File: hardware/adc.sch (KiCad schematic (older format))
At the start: 38 parts, among them U39 LP5907-3.0, U8 LTC2292

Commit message: Current working version.
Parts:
- removed C219, C30: 100n, fmcw3:C_0402b, symbol C
- C163, C164, C165, C166, C167, C168, C221, C223, C224, C225, C23, C24, C25, C27: footprint fmcw3:C_0402b -> Capacitor_SMD:C_0402_1005Metric; symbol C -> Device:C
- C19, C20, C216, C217, C218, C22, C220, C222, C249, C31: footprint fmcw3:C_0603b -> Capacitor_SMD:C_0603_1608Metric; symbol C -> Device:C
- C248: footprint fmcw3:C_0805b -> Capacitor_SMD:C_0805_2012Metric; symbol C -> Device:C
- R100, R20, R21, R91, R92, R93, R97, R98, R99: symbol R -> Device:R
- U39: symbol LP5907 -> fmcw3-rescue:LP5907
- U8: footprint Housings_DFN_QFN:QFN-64-1EP_9x9mm_Pitch0.5mm -> Package_DFN_QFN:QFN-64-1EP_9x9mm_P0.5mm_EP4.85x4.85mm; symbol LTC229X -> fmcw3-rescue:LTC229X
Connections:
- wire segments 120 -> 154

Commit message: Dropped the 3 from the end of the project name.
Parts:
- R100, R20, R21, R91, R92, R93, R97, R98, R99: footprint fmcw3:R_0402b -> fmcw:R_0402b
- U39: footprint fmcw3:SOT-23-5 -> fmcw:SOT-23-5; symbol fmcw3-rescue:LP5907 -> fmcw-rescue:LP5907-fmcw3-rescue
- U8: symbol fmcw3-rescue:LTC229X -> fmcw-rescue:LTC229X-fmcw3-rescue
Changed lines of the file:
@@
 EESchema Schematic File Version 4
-LIBS:fmcw3-cache
+LIBS:fmcw-cache
 EELAYER 26 0
 EELAYER END
@@
 F 0 "R93" V 4680 4950 50  0000 C CNN
 F 1 "0" V 4600 4950 50  0000 C CNN
-F 2 "fmcw3:R_0402b" V 4530 4950 30  0001 C CNN
+F 2 "fmcw:R_0402b" V 4530 4950 30  0001 C CNN
 F 3 "" H 4600 4950 30  0000 C CNN
 	1    4600 4950
@@
 F 0 "R91" V 2930 4700 50  0000 C CNN
 F 1 "0" V 2850 4700 50  0000 C CNN
-F 2 "fmcw3:R_0402b" V 2780 4700 30  0001 C CNN
+F 2 "fmcw:R_0402b" V 2780 4700 30  0001 C CNN
 F 3 "" H 2850 4700 30  0000 C CNN
 	1    2850 4700
@@
 F 0 "R92" V 2930 5100 50  0000 C CNN
 F 1 "DNP" V 2850 5100 50  0000 C CNN
-F 2 "fmcw3:R_0402b" V 2780 5100 30  0001 C CNN
+F 2 "fmcw:R_0402b" V 2780 5100 30  0001 C CNN
 F 3 "" H 2850 5100 30  0000 C CNN
 	1    2850 5100
@@
 OVDD
 $Comp
-L fmcw3-rescue:LP5907 U39
+L fmcw-rescue:LP5907-fmcw3-rescue U39
 U 1 1 58526584
 P 2800 1400
 F 0 "U39" H 3000 1200 60  0000 C CNN
 F 1 "LP5907-3.0" H 2900 1600 60  0000 C CNN
-F 2 "fmcw3:SOT-23-5" H 2800 1450 60  0001 C CNN
+F 2 "fmcw:SOT-23-5" H 2800 1450 60  0001 C CNN
 F 3 "" H 2800 1450 60  0000 C CNN
 	1    2800 1400
@@
 REFLA
 $Comp
-L fmcw3-rescue:LTC229X U8
+L fmcw-rescue:LTC229X-fmcw3-rescue U8
 U 1 1 59439276
 P 5950 4350
@@
 F 0 "R21" V 4680 3100 50  0000 C CNN
 F 1 "22" V 4600 3100 50  0000 C CNN
-F 2 "fmcw3:R_0402b" V 4530 3100 30  0001 C CNN
+F 2 "fmcw:R_0402b" V 4530 3100 30  0001 C CNN
 F 3 "" H 4600 3100 30  0000 C CNN
 	1    4600 3100
@@
 F 0 "R20" V 4430 5050 50  0000 C CNN
 F 1 "0" V 4350 5050 50  0000 C CNN
-F 2 "fmcw3:R_0402b" V 4280 5050 30  0001 C CNN
+F 2 "fmcw:R_0402b" V 4280 5050 30  0001 C CNN
 F 3 "" H 4350 5050 30  0000 C CNN
 	1    4350 5050
@@
 F 0 "R97" V 1430 2750 50  0000 C CNN
 F 1 "49.9" V 1350 2750 50  0000 C CNN
-F 2 "fmcw3:R_0402b" V 1280 2750 30  0001 C CNN
+F 2 "fmcw:R_0402b" V 1280 2750 30  0001 C CNN
 F 3 "" H 1350 2750 30  0000 C CNN
 	1    1350 2750
@@
 F 0 "R99" V 1730 2850 50  0000 C CNN
 F 1 "49.9" V 1650 2850 50  0000 C CNN
-F 2 "fmcw3:R_0402b" V 1580 2850 30  0001 C CNN
+F 2 "fmcw:R_0402b" V 1580 2850 30  0001 C CNN
 F 3 "" H 1650 2850 30  0000 C CNN
 	1    1650 2850
@@
 F 0 "R98" V 1430 4150 50  0000 C CNN
 F 1 "49.9" V 1350 4150 50  0000 C CNN
-F 2 "fmcw3:R_0402b" V 1280 4150 30  0001 C CNN
+F 2 "fmcw:R_0402b" V 1280 4150 30  0001 C CNN
 F 3 "" H 1350 4150 30  0000 C CNN
 	1    1350 4150
@@
 F 0 "R100" V 1730 4250 50  0000 C CNN
 F 1 "49.9" V 1650 4250 50  0000 C CNN
-F 2 "fmcw3:R_0402b" V 1580 4250 30  0001 C CNN
+F 2 "fmcw:R_0402b" V 1580 4250 30  0001 C CNN
 F 3 "" H 1650 4250 30  0000 C CNN
 	1    1650 4250

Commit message: Documentation for TPS5420D buck converter.
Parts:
- C248: MFN (none) -> 885012107014
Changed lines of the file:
@@
 F 2 "Capacitor_SMD:C_0805_2012Metric" H 1888 1400 30  0001 C CNN
 F 3 "" H 1850 1550 60  0000 C CNN
+F 4 "885012107014" H 0   0   50  0001 C CNN "MFN"
 	1    1850 1550
 	1    0    0    -1

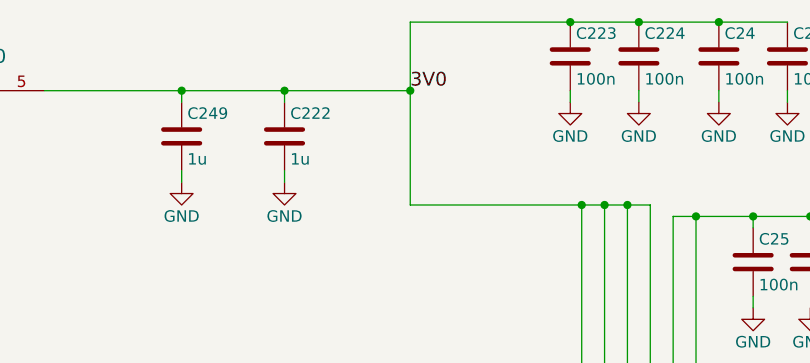
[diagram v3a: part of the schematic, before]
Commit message: Improved top level documentation.
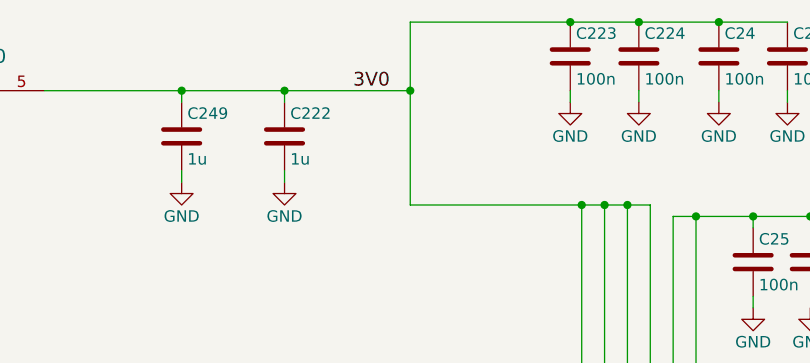
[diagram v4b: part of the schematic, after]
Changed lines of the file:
@@
 Text Label 2850 4450 0    60   ~ 0
 3V0
-Text Label 4900 1350 0    60   ~ 0
+Text Label 4650 1350 0    60   ~ 0
 3V0
 Text HLabel 7250 4100 2    60   Output ~ 0

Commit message: Added MFNs to components.
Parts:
- C163, C164, C165, C166, C167, C168: MFN (none) -> UMK105CG101JVHF
- C19, C20, C217, C218, C222, C249: MFN (none) -> CL10B105MO8NNWC
- C216, C22, C220, C31: MFN (none) -> CL10A225KO8NNNC
- C221, C223, C224, C225, C23, C24, C25, C27: MFN (none) -> CL05B104KO5NNNC
- C248: MFN 885012107014 -> CL21B106KQQNNNE
- R100, R97, R98, R99: footprint fmcw:R_0402b -> Resistor_SMD:R_0402_1005Metric; MFN (none) -> ERJ-2RKF49R9X
- R20, R91, R93: footprint fmcw:R_0402b -> Resistor_SMD:R_0402_1005Metric; MFN (none) -> ERJ-2GE0R00X
- R21: footprint fmcw:R_0402b -> Resistor_SMD:R_0402_1005Metric; MFN (none) -> ERJ-2RKF22R0X
- R92: footprint fmcw:R_0402b -> Resistor_SMD:R_0402_1005Metric
- U39: footprint fmcw:SOT-23-5 -> Package_TO_SOT_SMD:SOT-23-5; MFN (none) -> LP5907MFX-3.0/NOPB
- U8: MFN (none) -> LTC2292IUP#PBF
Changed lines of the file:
@@
 F 2 "Capacitor_SMD:C_0402_1005Metric" H 5638 1050 30  0001 C CNN
 F 3 "" H 5600 1200 60  0000 C CNN
+F 4 "CL05B104KO5NNNC" H 0   0   50  0001 C CNN "MFN"
 	1    5600 1200
 	1    0    0    -1
@@
 F 2 "Capacitor_SMD:C_0603_1608Metric" H 4388 1400 30  0001 C CNN
 F 3 "" H 4350 1550 60  0000 C CNN
+F 4 "CL10B105MO8NNWC" H 0   0   50  0001 C CNN "MFN"
 	1    4350 1550
 	1    0    0    -1
@@
 F 2 "Capacitor_SMD:C_0402_1005Metric" H 5938 1050 30  0001 C CNN
 F 3 "" H 5900 1200 60  0000 C CNN
+F 4 "CL05B104KO5NNNC" H 0   0   50  0001 C CNN "MFN"
 	1    5900 1200
 	1    0    0    -1
@@
 F 2 "Capacitor_SMD:C_0402_1005Metric" H 4438 3850 30  0001 C CNN
 F 3 "" H 4400 4000 60  0000 C CNN
+F 4 "CL05B104KO5NNNC" H 0   0   50  0001 C CNN "MFN"
 	1    4400 4000
 	1    0    0    -1
@@
 F 2 "Capacitor_SMD:C_0603_1608Metric" H 4188 3850 30  0001 C CNN
 F 3 "" H 4150 4000 60  0000 C CNN
+F 4 "CL10A225KO8NNNC" H 0   0   50  0001 C CNN "MFN"
 	1    4150 4000
 	1    0    0    -1
@@
 F 2 "Capacitor_SMD:C_0603_1608Metric" H 3788 3700 30  0001 C CNN
 F 3 "" H 3750 3850 60  0000 C CNN
+F 4 "CL10B105MO8NNWC" H 0   0   50  0001 C CNN "MFN"
 	1    3750 3850
 	0    1    1    0
@@
 F 2 "Capacitor_SMD:C_0603_1608Metric" H 3788 4000 30  0001 C CNN
 F 3 "" H 3750 4150 60  0000 C CNN
+F 4 "CL10B105MO8NNWC" H 0   0   50  0001 C CNN "MFN"
 	1    3750 4150
 	0    1    1    0
@@
 F 2 "Capacitor_SMD:C_0402_1005Metric" H 6688 1950 30  0001 C CNN
 F 3 "" H 6650 2100 60  0000 C CNN
+F 4 "CL05B104KO5NNNC" H 0   0   50  0001 C CNN "MFN"
 	1    6650 2100
 	1    0    0    -1
@@
 F 2 "Capacitor_SMD:C_0603_1608Metric" H 8588 4950 30  0001 C CNN
 F 3 "" H 8550 5100 60  0000 C CNN
+F 4 "CL10A225KO8NNNC" H 0   0   50  0001 C CNN "MFN"
 	1    8550 5100
 	-1   0    0    -1
@@
 F 0 "R93" V 4680 4950 50  0000 C CNN
 F 1 "0" V 4600 4950 50  0000 C CNN
-F 2 "fmcw:R_0402b" V 4530 4950 30  0001 C CNN
+F 2 "Resistor_SMD:R_0402_1005Metric" V 4530 4950 30  0001 C CNN
 F 3 "" H 4600 4950 30  0000 C CNN
+F 4 "ERJ-2GE0R00X" H 0   0   50  0001 C CNN "MFN"
 	1    4600 4950
 	0    1    1    0
@@
 F 0 "R91" V 2930 4700 50  0000 C CNN
 F 1 "0" V 2850 4700 50  0000 C CNN
-F 2 "fmcw:R_0402b" V 2780 4700 30  0001 C CNN
+F 2 "Resistor_SMD:R_0402_1005Metric" V 2780 4700 30  0001 C CNN
 F 3 "" H 2850 4700 30  0000 C CNN
+F 4 "ERJ-2GE0R00X" H 0   0   50  0001 C CNN "MFN"
 	1    2850 4700
 	1    0    0    -1
@@
 F 0 "R92" V 2930 5100 50  0000 C CNN
 F 1 "DNP" V 2850 5100 50  0000 C CNN
-F 2 "fmcw:R_0402b" V 2780 5100 30  0001 C CNN
+F 2 "Resistor_SMD:R_0402_1005Metric" V 2780 5100 30  0001 C CNN
 F 3 "" H 2850 5100 30  0000 C CNN
 	1    2850 5100
@@
 F 0 "U39" H 3000 1200 60  0000 C CNN
 F 1 "LP5907-3.0" H 2900 1600 60  0000 C CNN
-F 2 "fmcw:SOT-23-5" H 2800 1450 60  0001 C CNN
+F 2 "Package_TO_SOT_SMD:SOT-23-5" H 2800 1450 60  0001 C CNN
 F 3 "" H 2800 1450 60  0000 C CNN
+F 4 "LP5907MFX-3.0/NOPB" H 0   0   50  0001 C CNN "MFN"
 	1    2800 1400
 	1    0    0    -1
@@
 F 2 "Capacitor_SMD:C_0805_2012Metric" H 1888 1400 30  0001 C CNN
 F 3 "" H 1850 1550 60  0000 C CNN
-F 4 "885012107014" H 0   0   50  0001 C CNN "MFN"
+F 4 "CL21B106KQQNNNE" H 0   0   50  0001 C CNN "MFN"
 	1    1850 1550
 	1    0    0    -1
@@
 F 2 "Capacitor_SMD:C_0603_1608Metric" H 3938 1400 30  0001 C CNN
 F 3 "" H 3900 1550 60  0000 C CNN
+F 4 "CL10B105MO8NNWC" H 0   0   50  0001 C CNN "MFN"
 	1    3900 1550
 	1    0    0    -1
@@
 F 2 "Package_DFN_QFN:QFN-64-1EP_9x9mm_P0.5mm_EP4.85x4.85mm" H 3700 6300 60  0001 C CNN
 F 3 "http://www.analog.com/media/en/technical-documentation/data-sheets/229321fa.pdf" H 3700 6300 60  0001 C CNN
+F 4 "LTC2292IUP#PBF" H 0   0   50  0001 C CNN "MFN"
 	1    5950 4350
 	1    0    0    -1
@@
 F 2 "Capacitor_SMD:C_0402_1005Metric" H 4438 4350 30  0001 C CNN
 F 3 "" H 4400 4500 60  0000 C CNN
+F 4 "CL05B104KO5NNNC" H 0   0   50  0001 C CNN "MFN"
 	1    4400 4500
 	1    0    0    -1
@@
 F 2 "Capacitor_SMD:C_0603_1608Metric" H 4188 4350 30  0001 C CNN
 F 3 "" H 4150 4500 60  0000 C CNN
+F 4 "CL10A225KO8NNNC" H 0   0   50  0001 C CNN "MFN"
 	1    4150 4500
 	1    0    0    -1
@@
 F 2 "Capacitor_SMD:C_0603_1608Metric" H 3788 4200 30  0001 C CNN
 F 3 "" H 3750 4350 60  0000 C CNN
+F 4 "CL10B105MO8NNWC" H 0   0   50  0001 C CNN "MFN"
 	1    3750 4350
 	0    1    1    0
@@
 F 2 "Capacitor_SMD:C_0603_1608Metric" H 3788 4500 30  0001 C CNN
 F 3 "" H 3750 4650 60  0000 C CNN
+F 4 "CL10B105MO8NNWC" H 0   0   50  0001 C CNN "MFN"
 	1    3750 4650
 	0    1    1    0
@@
 F 2 "Capacitor_SMD:C_0402_1005Metric" H 6288 1050 30  0001 C CNN
 F 3 "" H 6250 1200 60  0000 C CNN
+F 4 "CL05B104KO5NNNC" H 0   0   50  0001 C CNN "MFN"
 	1    6250 1200
 	1    0    0    -1
@@
 F 2 "Capacitor_SMD:C_0402_1005Metric" H 6588 1050 30  0001 C CNN
 F 3 "" H 6550 1200 60  0000 C CNN
+F 4 "CL05B104KO5NNNC" H 0   0   50  0001 C CNN "MFN"
 	1    6550 1200
 	1    0    0    -1
@@
 F 2 "Capacitor_SMD:C_0402_1005Metric" H 6438 1950 30  0001 C CNN
 F 3 "" H 6400 2100 60  0000 C CNN
+F 4 "CL05B104KO5NNNC" H 0   0   50  0001 C CNN "MFN"
 	1    6400 2100
 	1    0    0    -1
@@
 F 2 "Capacitor_SMD:C_0603_1608Metric" H 8538 5750 30  0001 C CNN
 F 3 "" H 8500 5900 60  0000 C CNN
+F 4 "CL10A225KO8NNNC" H 0   0   50  0001 C CNN "MFN"
 	1    8500 5900
 	-1   0    0    -1
@@
 F 0 "R21" V 4680 3100 50  0000 C CNN
 F 1 "22" V 4600 3100 50  0000 C CNN
-F 2 "fmcw:R_0402b" V 4530 3100 30  0001 C CNN
+F 2 "Resistor_SMD:R_0402_1005Metric" V 4530 3100 30  0001 C CNN
 F 3 "" H 4600 3100 30  0000 C CNN
+F 4 "ERJ-2RKF22R0X" H 0   0   50  0001 C CNN "MFN"
 	1    4600 3100
 	0    1    1    0
@@
 F 0 "R20" V 4430 5050 50  0000 C CNN
 F 1 "0" V 4350 5050 50  0000 C CNN
-F 2 "fmcw:R_0402b" V 4280 5050 30  0001 C CNN
+F 2 "Resistor_SMD:R_0402_1005Metric" V 4280 5050 30  0001 C CNN
 F 3 "" H 4350 5050 30  0000 C CNN
+F 4 "ERJ-2GE0R00X" H 0   0   50  0001 C CNN "MFN"
 	1    4350 5050
 	0    1    1    0
@@
 F 0 "R97" V 1430 2750 50  0000 C CNN
 F 1 "49.9" V 1350 2750 50  0000 C CNN
-F 2 "fmcw:R_0402b" V 1280 2750 30  0001 C CNN
+F 2 "Resistor_SMD:R_0402_1005Metric" V 1280 2750 30  0001 C CNN
 F 3 "" H 1350 2750 30  0000 C CNN
+F 4 "ERJ-2RKF49R9X" H 0   0   50  0001 C CNN "MFN"
 	1    1350 2750
 	0    1    1    0
@@
 F 0 "R99" V 1730 2850 50  0000 C CNN
 F 1 "49.9" V 1650 2850 50  0000 C CNN
-F 2 "fmcw:R_0402b" V 1580 2850 30  0001 C CNN
+F 2 "Resistor_SMD:R_0402_1005Metric" V 1580 2850 30  0001 C CNN
 F 3 "" H 1650 2850 30  0000 C CNN
+F 4 "ERJ-2RKF49R9X" H 0   0   50  0001 C CNN "MFN"
 	1    1650 2850
 	0    1    1    0
@@
 F 2 "Capacitor_SMD:C_0402_1005Metric" H 2088 2650 30  0001 C CNN
 F 3 "" H 2050 2800 60  0000 C CNN
+F 4 "UMK105CG101JVHF" H 0   0   50  0001 C CNN "MFN"
 	1    2050 2800
 	1    0    0    -1
@@
 F 2 "Capacitor_SMD:C_0402_1005Metric" H 2088 2300 30  0001 C CNN
 F 3 "" H 2050 2450 60  0000 C CNN
+F 4 "UMK105CG101JVHF" H 0   0   50  0001 C CNN "MFN"
 	1    2050 2450
 	1    0    0    -1
@@
 F 2 "Capacitor_SMD:C_0402_1005Metric" H 2088 3000 30  0001 C CNN
 F 3 "" H 2050 3150 60  0000 C CNN
+F 4 "UMK105CG101JVHF" H 0   0   50  0001 C CNN "MFN"
 	1    2050 3150
 	1    0    0    -1
@@
 F 0 "R98" V 1430 4150 50  0000 C CNN
 F 1 "49.9" V 1350 4150 50  0000 C CNN
-F 2 "fmcw:R_0402b" V 1280 4150 30  0001 C CNN
+F 2 "Resistor_SMD:R_0402_1005Metric" V 1280 4150 30  0001 C CNN
 F 3 "" H 1350 4150 30  0000 C CNN
+F 4 "ERJ-2RKF49R9X" H 0   0   50  0001 C CNN "MFN"
 	1    1350 4150
 	0    1    1    0
@@
 F 0 "R100" V 1730 4250 50  0000 C CNN
 F 1 "49.9" V 1650 4250 50  0000 C CNN
-F 2 "fmcw:R_0402b" V 1580 4250 30  0001 C CNN
+F 2 "Resistor_SMD:R_0402_1005Metric" V 1580 4250 30  0001 C CNN
 F 3 "" H 1650 4250 30  0000 C CNN
+F 4 "ERJ-2RKF49R9X" H 0   0   50  0001 C CNN "MFN"
 	1    1650 4250
 	0    1    1    0
@@
 F 2 "Capacitor_SMD:C_0402_1005Metric" H 2088 4050 30  0001 C CNN
 F 3 "" H 2050 4200 60  0000 C CNN
+F 4 "UMK105CG101JVHF" H 0   0   50  0001 C CNN "MFN"
 	1    2050 4200
 	1    0    0    -1
@@
 F 2 "Capacitor_SMD:C_0402_1005Metric" H 2088 3700 30  0001 C CNN
 F 3 "" H 2050 3850 60  0000 C CNN
+F 4 "UMK105CG101JVHF" H 0   0   50  0001 C CNN "MFN"
 	1    2050 3850
 	1    0    0    -1
@@
 F 2 "Capacitor_SMD:C_0402_1005Metric" H 2088 4400 30  0001 C CNN
 F 3 "" H 2050 4550 60  0000 C CNN
+F 4 "UMK105CG101JVHF" H 0   0   50  0001 C CNN "MFN"
 	1    2050 4550
 	1    0    0    -1

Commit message: Improved documentation and added schematics to default libraries.
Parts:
- U39: symbol fmcw-rescue:LP5907-fmcw3-rescue -> Regulator_Linear:LP5907MFX-3.0
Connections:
- net GND: no longer U39.2 (GND)
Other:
- moved on the sheet: C248, U39
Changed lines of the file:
@@
 U 1 1 583E665A
 P 3750 3850
-F 0 "C217" H 3775 3950 50  0000 L CNN
-F 1 "1u" H 3775 3750 50  0000 L CNN
+F 0 "C217" V 3800 3600 50  0000 L CNN
+F 1 "1u" V 3700 3700 50  0000 L CNN
 F 2 "Capacitor_SMD:C_0603_1608Metric" H 3788 3700 30  0001 C CNN
 F 3 "" H 3750 3850 60  0000 C CNN
@@
 U 1 1 583E669C
 P 3750 4150
-F 0 "C218" H 3775 4250 50  0000 L CNN
-F 1 "1u" H 3775 4050 50  0000 L CNN
+F 0 "C218" V 3800 3900 50  0000 L CNN
+F 1 "1u" V 3700 4000 50  0000 L CNN
 F 2 "Capacitor_SMD:C_0603_1608Metric" H 3788 4000 30  0001 C CNN
 F 3 "" H 3750 4150 60  0000 C CNN
@@
 U 1 1 583EA63A
 P 2850 4700
-F 0 "R91" V 2930 4700 50  0000 C CNN
-F 1 "0" V 2850 4700 50  0000 C CNN
+F 0 "R91" H 2920 4746 50  0000 L CNN
+F 1 "0" H 2920 4655 50  0000 L CNN
 F 2 "Resistor_SMD:R_0402_1005Metric" V 2780 4700 30  0001 C CNN
 F 3 "" H 2850 4700 30  0000 C CNN
@@
 U 1 1 583EA67C
 P 2850 5100
-F 0 "R92" V 2930 5100 50  0000 C CNN
-F 1 "DNP" V 2850 5100 50  0000 C CNN
+F 0 "R92" H 2920 5146 50  0000 L CNN
+F 1 "DNP" H 2920 5055 50  0000 L CNN
 F 2 "Resistor_SMD:R_0402_1005Metric" V 2780 5100 30  0001 C CNN
 F 3 "" H 2850 5100 30  0000 C CNN
@@
 OVDD
 $Comp
-L fmcw-rescue:LP5907-fmcw3-rescue U39
+L Regulator_Linear:LP5907MFX-3.0 U39
 U 1 1 58526584
-P 2800 1400
-F 0 "U39" H 3000 1200 60  0000 C CNN
-F 1 "LP5907-3.0" H 2900 1600 60  0000 C CNN
-F 2 "Package_TO_SOT_SMD:SOT-23-5" H 2800 1450 60  0001 C CNN
-F 3 "" H 2800 1450 60  0000 C CNN
-F 4 "LP5907MFX-3.0/NOPB" H 0   0   50  0001 C CNN "MFN"
-	1    2800 1400
+P 3000 1450
+F 0 "U39" H 3000 1839 60  0000 C CNN
+F 1 "LP5907-3.0" H 3000 1733 60  0000 C CNN
+F 2 "Package_TO_SOT_SMD:SOT-23-5" H 3000 1500 60  0001 C CNN
+F 3 "" H 3000 1500 60  0000 C CNN
+F 4 "LP5907MFX-3.0/NOPB" H 200 50  50  0001 C CNN "MFN"
+	1    3000 1450
 	1    0    0    -1
 $EndComp
@@
 L power:GND #PWR071
 U 1 1 585266D4
-P 2800 1750
-F 0 "#PWR071" H 2800 1500 50  0001 C CNN
-F 1 "GND" H 2800 1600 50  0000 C CNN
-F 2 "" H 2800 1750 60  0000 C CNN
-F 3 "" H 2800 1750 60  0000 C CNN
-	1    2800 1750
-	1    0    0    -1
-$EndComp
-Wire Wire Line
-	2300 1450 2200 1450
-Wire Wire Line
-	2200 1450 2200 1350
-Wire Wire Line
-	1750 1350 1850 1350
+P 3000 1800
+F 0 "#PWR071" H 3000 1550 50  0001 C CNN
+F 1 "GND" H 3000 1650 50  0000 C CNN
+F 2 "" H 3000 1800 60  0000 C CNN
+F 3 "" H 3000 1800 60  0000 C CNN
+	1    3000 1800
+	1    0    0    -1
+$EndComp
+Wire Wire Line
+	2700 1450 2600 1450
+Wire Wire Line
+	2600 1450 2600 1350
+Wire Wire Line
+	2150 1350 2250 1350
 $Comp
 L Device:C C248
 U 1 1 5852675F
-P 1850 1550
-F 0 "C248" H 1875 1650 50  0000 L CNN
-F 1 "10u" H 1875 1450 50  0000 L CNN
-F 2 "Capacitor_SMD:C_0805_2012Metric" H 1888 1400 30  0001 C CNN
-F 3 "" H 1850 1550 60  0000 C CNN
-F 4 "CL21B106KQQNNNE" H 0   0   50  0001 C CNN "MFN"
-	1    1850 1550
+P 2250 1550
+F 0 "C248" H 2275 1650 50  0000 L CNN
+F 1 "10u" H 2275 1450 50  0000 L CNN
+F 2 "Capacitor_SMD:C_0805_2012Metric" H 2288 1400 30  0001 C CNN
+F 3 "" H 2250 1550 60  0000 C CNN
+F 4 "CL21B106KQQNNNE" H 400 0   50  0001 C CNN "MFN"
+	1    2250 1550
 	1    0    0    -1
 $EndComp
@@
 L power:GND #PWR072
 U 1 1 585267C4
-P 1850 1700
-F 0 "#PWR072" H 1850 1450 50  0001 C CNN
-F 1 "GND" H 1850 1550 50  0000 C CNN
-F 2 "" H 1850 1700 60  0000 C CNN
-F 3 "" H 1850 1700 60  0000 C CNN
-	1    1850 1700
-	1    0    0    -1
-$EndComp
-Wire Wire Line
-	1850 1400 1850 1350
-Connection ~ 2200 1350
-Connection ~ 1850 1350
-Text HLabel 1750 1350 0    60   Input ~ 0
+P 2250 1700
+F 0 "#PWR072" H 2250 1450 50  0001 C CNN
+F 1 "GND" H 2250 1550 50  0000 C CNN
+F 2 "" H 2250 1700 60  0000 C CNN
+F 3 "" H 2250 1700 60  0000 C CNN
+	1    2250 1700
+	1    0    0    -1
+$EndComp
+Wire Wire Line
+	2250 1400 2250 1350
+Connection ~ 2600 1350
+Connection ~ 2250 1350
+Text HLabel 2150 1350 0    60   Input ~ 0
 3V6
 $Comp
@@
 U 1 1 5943A0B5
 P 3750 4350
-F 0 "C19" H 3775 4450 50  0000 L CNN
-F 1 "1u" H 3775 4250 50  0000 L CNN
+F 0 "C19" V 3800 4150 50  0000 L CNN
+F 1 "1u" V 3700 4200 50  0000 L CNN
 F 2 "Capacitor_SMD:C_0603_1608Metric" H 3788 4200 30  0001 C CNN
 F 3 "" H 3750 4350 60  0000 C CNN
@@
 U 1 1 5943A0BB
 P 3750 4650
-F 0 "C20" H 3775 4750 50  0000 L CNN
-F 1 "1u" H 3775 4550 50  0000 L CNN
+F 0 "C20" V 3800 4450 50  0000 L CNN
+F 1 "1u" V 3700 4500 50  0000 L CNN
 F 2 "Capacitor_SMD:C_0603_1608Metric" H 3788 4500 30  0001 C CNN
 F 3 "" H 3750 4650 60  0000 C CNN
@@
 U 1 1 596FAE3E
 P 1350 2750
-F 0 "R97" V 1430 2750 50  0000 C CNN
-F 1 "49.9" V 1350 2750 50  0000 C CNN
+F 0 "R97" V 1143 2750 50  0000 C CNN
+F 1 "49.9" V 1234 2750 50  0000 C CNN
 F 2 "Resistor_SMD:R_0402_1005Metric" V 1280 2750 30  0001 C CNN
 F 3 "" H 1350 2750 30  0000 C CNN
@@
 U 1 1 596FAF3C
 P 1650 2850
-F 0 "R99" V 1730 2850 50  0000 C CNN
-F 1 "49.9" V 1650 2850 50  0000 C CNN
+F 0 "R99" V 1765 2850 50  0000 C CNN
+F 1 "49.9" V 1856 2850 50  0000 C CNN
 F 2 "Resistor_SMD:R_0402_1005Metric" V 1580 2850 30  0001 C CNN
 F 3 "" H 1650 2850 30  0000 C CNN
@@
 U 1 1 596FB1DA
 P 2050 2800
-F 0 "C164" H 2075 2900 50  0000 L CNN
-F 1 "100p" H 2075 2700 50  0000 L CNN
+F 0 "C164" H 2165 2846 50  0000 L CNN
+F 1 "100p" H 2165 2755 50  0000 L CNN
 F 2 "Capacitor_SMD:C_0402_1005Metric" H 2088 2650 30  0001 C CNN
 F 3 "" H 2050 2800 60  0000 C CNN
@@
 U 1 1 596FB23D
 P 2050 2450
-F 0 "C163" H 2075 2550 50  0000 L CNN
-F 1 "100p" H 2075 2350 50  0000 L CNN
+F 0 "C163" H 2165 2496 50  0000 L CNN
+F 1 "100p" H 2165 2405 50  0000 L CNN
 F 2 "Capacitor_SMD:C_0402_1005Metric" H 2088 2300 30  0001 C CNN
 F 3 "" H 2050 2450 60  0000 C CNN
@@
 U 1 1 596FB297
 P 2050 3150
-F 0 "C165" H 2075 3250 50  0000 L CNN
-F 1 "100p" H 2075 3050 50  0000 L CNN
+F 0 "C165" H 2165 3196 50  0000 L CNN
+F 1 "100p" H 2165 3105 50  0000 L CNN
 F 2 "Capacitor_SMD:C_0402_1005Metric" H 2088 3000 30  0001 C CNN
 F 3 "" H 2050 3150 60  0000 C CNN
@@
 U 1 1 596FBF21
 P 1350 4150
-F 0 "R98" V 1430 4150 50  0000 C CNN
-F 1 "49.9" V 1350 4150 50  0000 C CNN
+F 0 "R98" V 1143 4150 50  0000 C CNN
+F 1 "49.9" V 1234 4150 50  0000 C CNN
 F 2 "Resistor_SMD:R_0402_1005Metric" V 1280 4150 30  0001 C CNN
 F 3 "" H 1350 4150 30  0000 C CNN
@@
 U 1 1 596FBF28
 P 1650 4250
-F 0 "R100" V 1730 4250 50  0000 C CNN
-F 1 "49.9" V 1650 4250 50  0000 C CNN
+F 0 "R100" V 1765 4250 50  0000 C CNN
+F 1 "49.9" V 1856 4250 50  0000 C CNN
 F 2 "Resistor_SMD:R_0402_1005Metric" V 1580 4250 30  0001 C CNN
 F 3 "" H 1650 4250 30  0000 C CNN
@@
 U 1 1 596FBF30
 P 2050 4200
-F 0 "C167" H 2075 4300 50  0000 L CNN
-F 1 "100p" H 2075 4100 50  0000 L CNN
+F 0 "C167" H 2165 4246 50  0000 L CNN
+F 1 "100p" H 2165 4155 50  0000 L CNN
 F 2 "Capacitor_SMD:C_0402_1005Metric" H 2088 4050 30  0001 C CNN
 F 3 "" H 2050 4200 60  0000 C CNN
@@
 U 1 1 596FBF37
 P 2050 3850
-F 0 "C166" H 2075 3950 50  0000 L CNN
-F 1 "100p" H 2075 3750 50  0000 L CNN
+F 0 "C166" H 2165 3896 50  0000 L CNN
+F 1 "100p" H 2165 3805 50  0000 L CNN
 F 2 "Capacitor_SMD:C_0402_1005Metric" H 2088 3700 30  0001 C CNN
 F 3 "" H 2050 3850 60  0000 C CNN
@@
 U 1 1 596FBF3E
 P 2050 4550
-F 0 "C168" H 2075 4650 50  0000 L CNN
-F 1 "100p" H 2075 4450 50  0000 L CNN
+F 0 "C168" H 2165 4596 50  0000 L CNN
+F 1 "100p" H 2165 4505 50  0000 L CNN
 F 2 "Capacitor_SMD:C_0402_1005Metric" H 2088 4400 30  0001 C CNN
 F 3 "" H 2050 4550 60  0000 C CNN
@@
 	8550 4850 8750 4850
 Wire Wire Line
-	2200 1350 2300 1350
-Wire Wire Line
-	1850 1350 2200 1350
+	2600 1350 2700 1350
+Wire Wire Line
+	2250 1350 2600 1350
 Wire Wire Line
 	3900 1350 4350 1350
